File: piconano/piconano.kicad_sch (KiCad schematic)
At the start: 3 parts, among them SW1 SW_Push, SW2 SW_Push

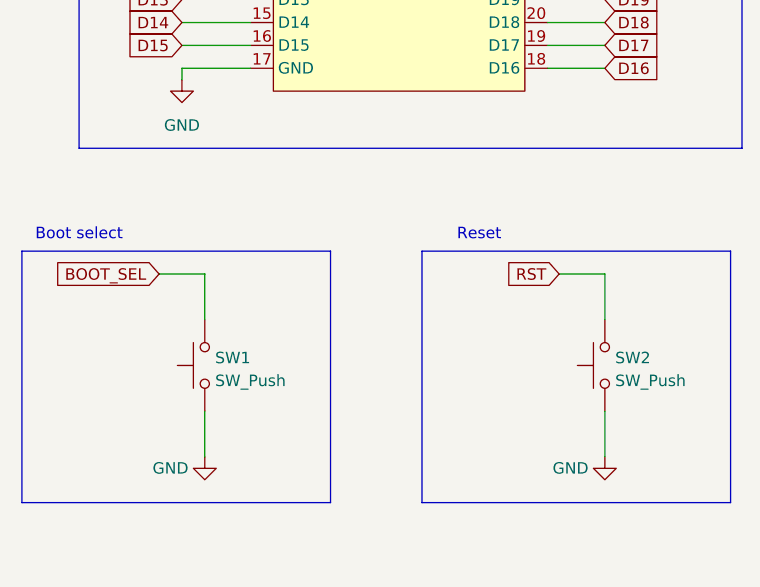
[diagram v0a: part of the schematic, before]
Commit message: update to new lib structure and to V10
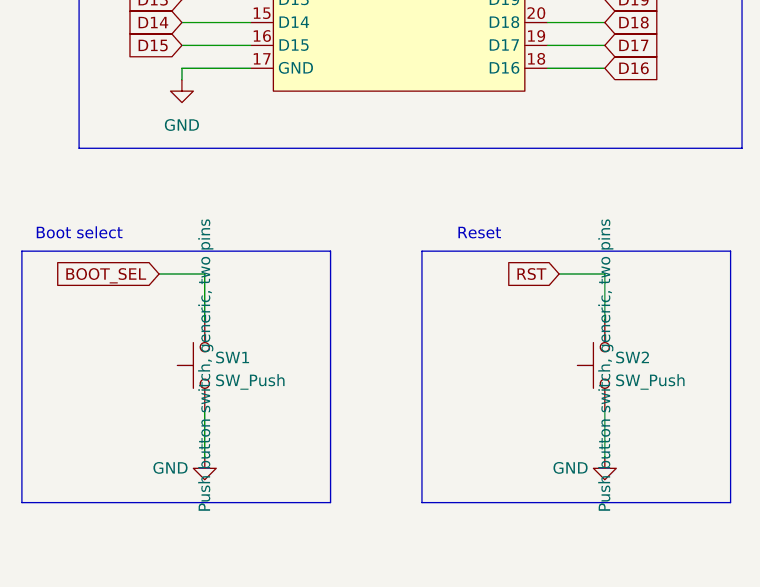
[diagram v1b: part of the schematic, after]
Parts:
- J2: value ~ -> (none)
